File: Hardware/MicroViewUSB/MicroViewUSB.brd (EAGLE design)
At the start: 27.9 x 20.3 mm, 26 parts, among them J1 MICROVIEW-16ND, Q1 2N7002PW, U1 FT231XS

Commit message: Adding fids to both boards
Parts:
- added FID1, FID2: FIDUCIAL1X2, SparkFun-Aesthetics:FIDUCIAL-1X2
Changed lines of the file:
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@@
 <element name="LOGO2" library="SparkFun-Aesthetics" package="SFE_LOGO_FLAME_.1" value="SFE_LOGO_FLAME.1_INCH" x="4.445" y="16.764"/>
 <element name="LOGO3" library="SparkFun-Aesthetics" package="SFE_LOGO_NAME_FLAME_.1" value="SFE_LOGO_NAME_FLAME.1_INCH" x="21.59" y="11.43" rot="MR0"/>
+<element name="FID1" library="SparkFun-Aesthetics" package="FIDUCIAL-1X2" value="FIDUCIAL1X2" x="4.826" y="1.143"/>
+<element name="FID2" library="SparkFun-Aesthetics" package="FIDUCIAL-1X2" value="FIDUCIAL1X2" x="25.4" y="18.161"/>
 </elements>
 <signals>

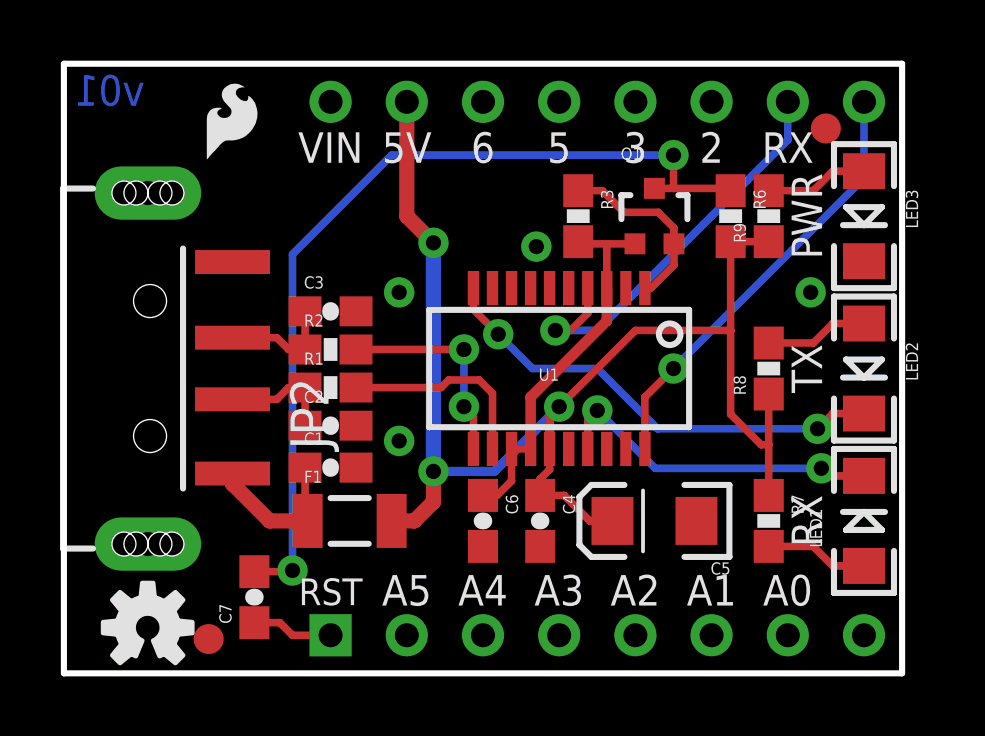
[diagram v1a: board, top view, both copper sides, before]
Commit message: Staggering/increasing drill on headers
Also spacing out resistors, increasing header fp on MicroViewUSB.
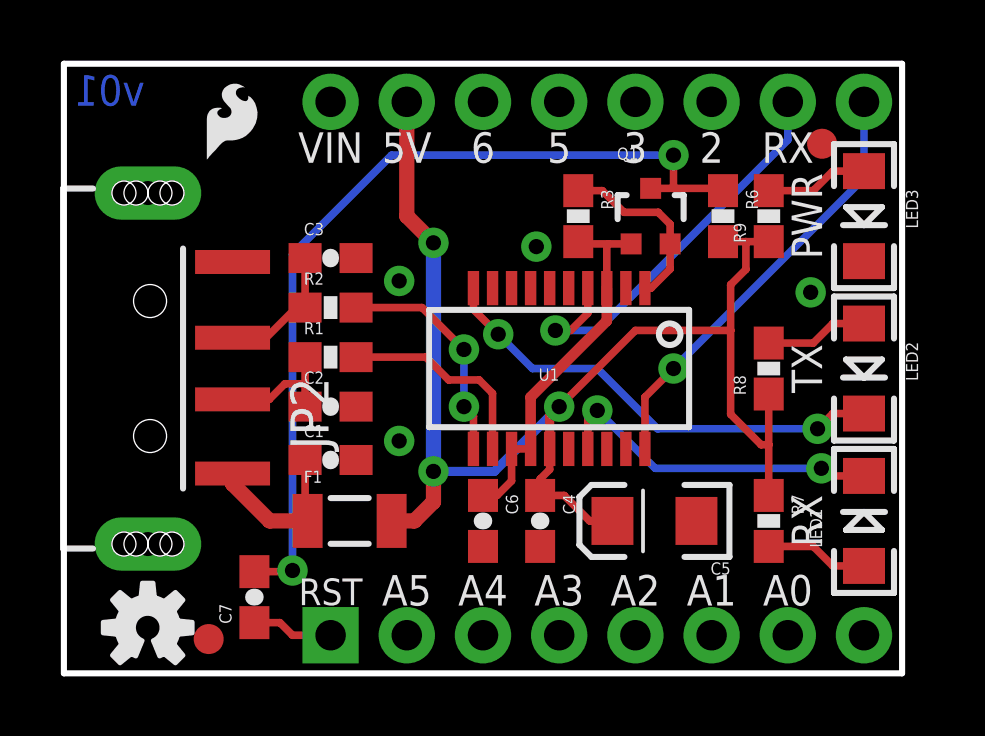
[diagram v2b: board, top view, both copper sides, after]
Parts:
- moved C3 1.78 mm to (8.89, 13.8)
- moved R2 1.40 mm to (8.89, 12.2)
- moved R1 1.02 mm to (8.89, 10.5)
- moved C2 0.63 mm to (8.89, 8.89)
- moved FID2 0.52 mm to (25.3, 17.7)
- moved R6 0.25 mm to (22.0, 15.2)
- moved C1 0.25 mm to (8.89, 7.11)
- moved Q1 0.13 mm to (19.6, 15.2)
- renumbered J1 to J2
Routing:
- net D+: track 3.85 -> 4.91 mm
- net N$7: track 7.04 -> 7.62 mm

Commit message: Updating r's and c's on USB board to prod. parts
Also rearranging some silk and traces.
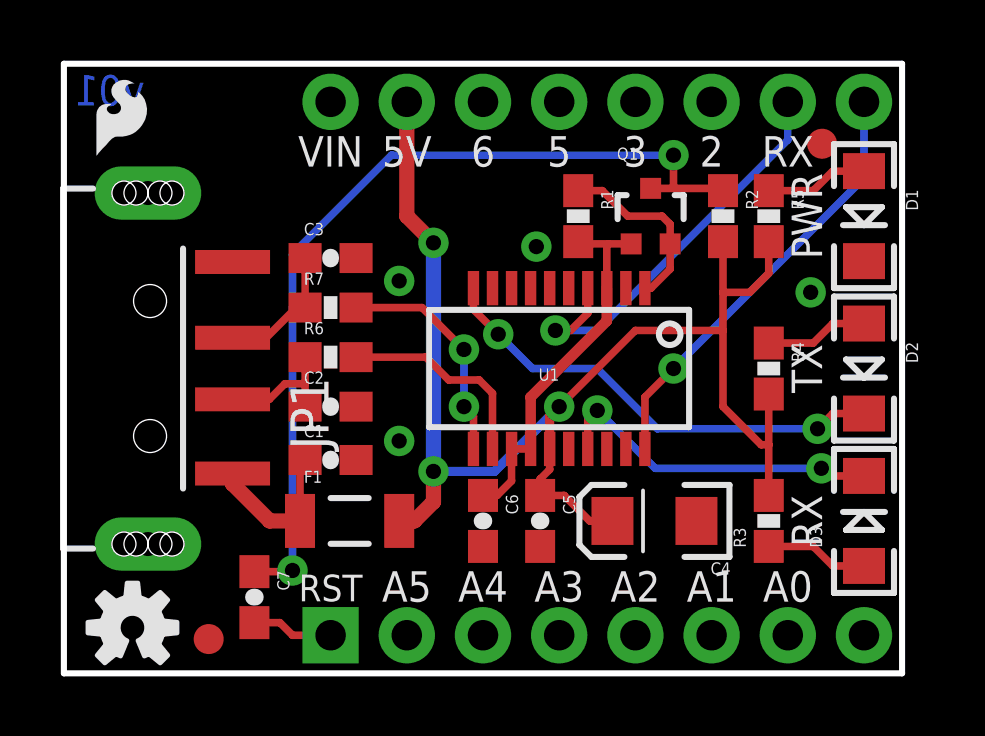
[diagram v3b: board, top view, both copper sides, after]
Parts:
- removed R8, R9: 1k, SparkFun:0603-RES
- added R4, R5: 1K, SparkFun-Resistors:0603-RES
- C1, C6: device SparkFun:0603-CAP -> SparkFun-Capacitors:0603-CAP
- C4: value 0.1uF -> 10uF; device SparkFun:0603-CAP -> SparkFun-Capacitors:EIA3216
- C5: value 10uF -> 0.1uF; device SparkFun-Capacitors:EIA3216 -> SparkFun-Capacitors:0603-CAP
- D1: value Green -> GREEN
- D2: value Red -> RED
- F1: device SparkFun:PTC-1206 -> SparkFun-PowerIC:PTC-1206-WIDE
- LOGO1: value OSHW-LOGOS -> SFE_LOGO_FLAME.1_INCH; device SparkFun-Aesthetics:OSHW-LOGO-S -> SparkFun-Aesthetics:SFE_LOGO_FLAME_.1
- LOGO2: value SFE_LOGO_FLAME.1_INCH -> OSHW-LOGOS; device SparkFun-Aesthetics:SFE_LOGO_FLAME_.1 -> SparkFun-Aesthetics:OSHW-LOGO-S
- R1, R2: value 27 -> 10K
- R3: value 10k -> 1K; device SparkFun:0603-RES -> SparkFun-Resistors:0603-RES
- R6: value 10k -> 27; device SparkFun:0603-RES -> SparkFun-Resistors:0603-RES
- R7: value 1k -> 27; device SparkFun:0603-RES -> SparkFun-Resistors:0603-RES
- moved R7 16.2 mm to (8.89, 12.2), turned to 0 degrees
- moved LOGO1 15.5 mm to (0.76, 16.9)
- moved LOGO2 15.4 mm to (2.29, 1.52)
- moved R6 13.9 mm to (8.89, 10.5), turned to 0 degrees
- moved R2 13.4 mm to (22.0, 15.2), turned to 270 degrees
- moved R3 12.0 mm to (23.5, 5.08), turned to 90 degrees
- moved R1 9.50 mm to (17.1, 15.2), turned to 270 degrees
- moved C4 3.81 mm to (19.7, 5.08), turned to 180 degrees
- moved C5 3.81 mm to (15.9, 5.08), turned to 270 degrees
- turned C7 to 270 degrees
- renumbered J2 to J1, JP2 to JP1, LED1 to D3, LED2 to D2, LED3 to D1
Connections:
- net 3.3V: now also R1.2; no longer R3.2
- net 5V: now also C4.A, C5.1, R2.2, R3.2, R4.2, R5.2; no longer C4.1, C5.A, R6.2, R7.1, R8.1, R9.1
- net D+: now also R7.1; no longer R2.1
- net D-: now also R6.1; no longer R1.1
- net DTR: now also C7.1, R2.1; no longer C7.2, R6.1
- net GND: now also C4.C, C5.2; no longer C4.2, C5.C
- net N$1: now also R5.1; no longer R9.2
- net N$10: now also R3.1; no longer R7.2
- net N$12: now also R1.1; no longer R3.1
- net N$2: now also C7.2; no longer C7.1
- net N$6: now also R6.2; no longer R1.2
- net N$7: now also R7.2; no longer R2.2
- net N$8: now also R4.1; no longer R8.2
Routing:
- net 5V: track 45.8 -> 46.5 mm
